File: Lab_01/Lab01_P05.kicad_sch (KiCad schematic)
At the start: 4 parts

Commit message: Edit Lab01 P5 Simulation
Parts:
- removed RLOAD1: 1000, symbol Device:R_Variable
- added R3: 1000, symbol Device:R
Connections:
- net GND: now also R3.2
- net Vout: now also R3.1
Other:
- note removed: ".tran 1u 1m"
- moved on the sheet: R1, R2, V_SUPPLY1

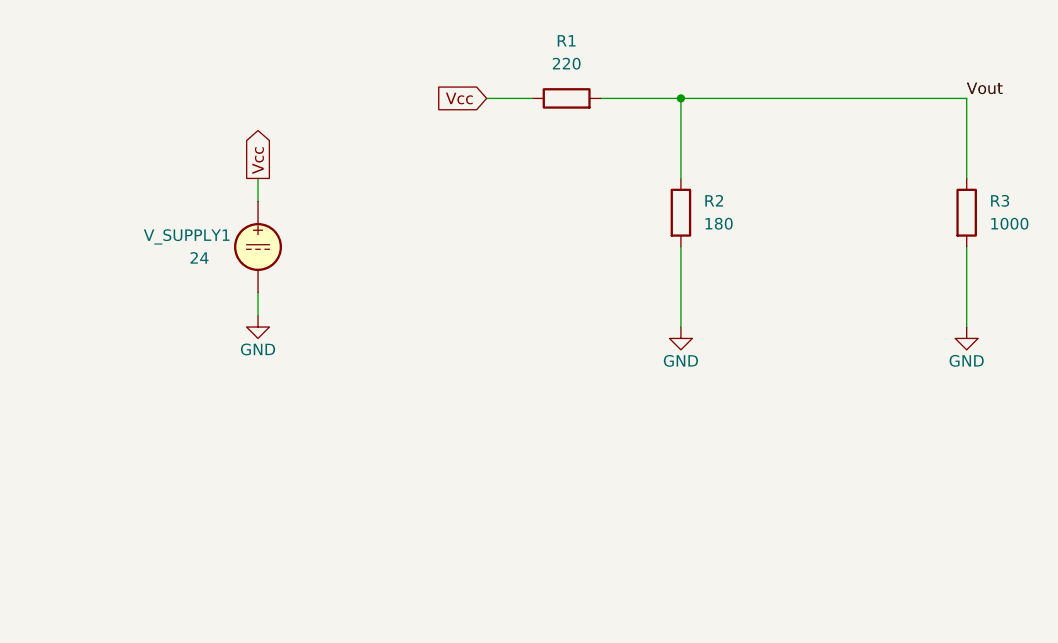
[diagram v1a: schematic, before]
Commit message: Capture and simulate P6&7 schemas
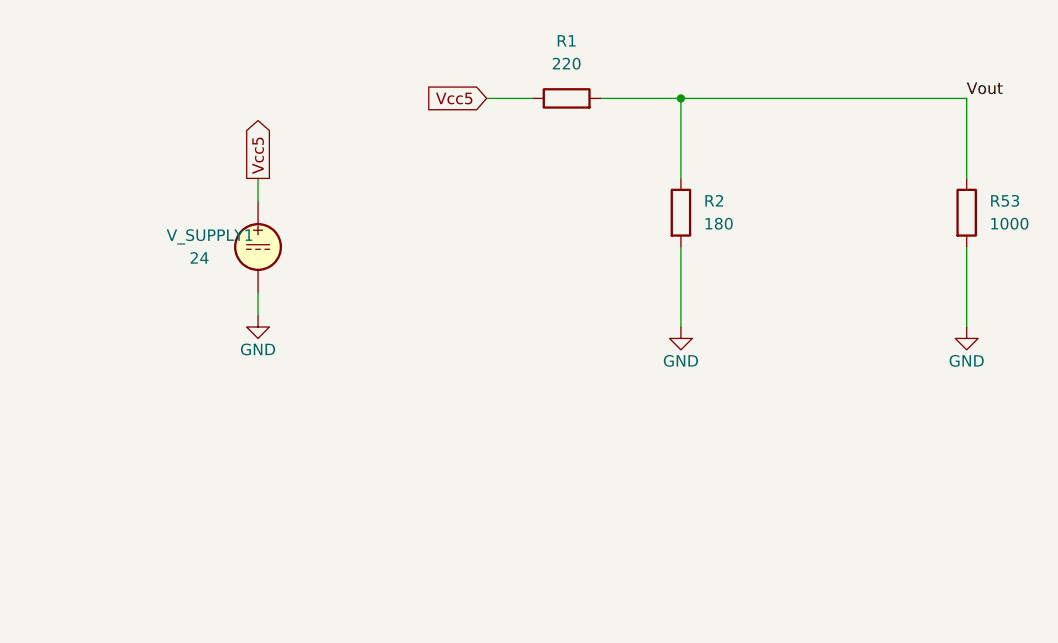
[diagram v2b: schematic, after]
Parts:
- renumbered R3 to R53
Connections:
- net Vcc renamed Vcc5
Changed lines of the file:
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@@
     (effects (font (size 1.27 1.27)) (justify left bottom))
   )
-  (global_label "Vcc" (shape output) (at 41.91 48.26 90) (fields_autoplaced)
+  (global_label "Vcc5" (shape output) (at 41.91 48.26 90) (fields_autoplaced)
     (effects (font (size 1.27 1.27)) (justify left))
-    (property "Intersheetrefs" "${INTERSHEET_REFS}" (at 41.91 42.0884 90)
+    (property "Intersheetrefs" "${INTERSHEET_REFS}" (at 41.91 40.8789 90)
       (effects (font (size 1.27 1.27)) (justify left) hide)
     )
   )
-  (global_label "Vcc" (shape input) (at 67.31 39.37 180) (fields_autoplaced)
+  (global_label "Vcc5" (shape input) (at 67.31 39.37 180) (fields_autoplaced)
     (effects (font (size 1.27 1.27)) (justify right))
-    (property "Intersheetrefs" "${INTERSHEET_REFS}" (at 61.1384 39.37 0)
+    (property "Intersheetrefs" "${INTERSHEET_REFS}" (at 59.9289 39.37 0)
       (effects (font (size 1.27 1.27)) (justify right) hide)
     )
@@
   (symbol (lib_id "Simulation_SPICE:VDC") (at 41.91 55.88 0) (unit 1)
     (in_bom yes) (on_board yes) (dnp no)
-    (property "Reference" "V_SUPPLY1" (at 29.21 54.61 0)
+    (property "Reference" "V_SUPPLY1" (at 31.75 54.61 0)
       (effects (font (size 1.27 1.27)) (justify left))
     )
@@
       (project "Lab01"
         (path "/f5e37932-d66b-45bd-afc2-f24a1a74700d/4efdc02f-e125-44e1-b96d-4aab0a060814"
-          (reference "V_SUPPLY1") (unit 1)
+          (reference "VDC51") (unit 1)
         )
       )
@@
   (symbol (lib_id "Device:R") (at 120.65 52.07 0) (unit 1)
     (in_bom yes) (on_board yes) (dnp no) (fields_autoplaced)
-    (property "Reference" "R3" (at 123.19 50.8 0)
+    (property "Reference" "R53" (at 123.19 50.8 0)
       (effects (font (size 1.27 1.27)) (justify left))
     )
@@
       (project "Lab01"
         (path "/f5e37932-d66b-45bd-afc2-f24a1a74700d/4efdc02f-e125-44e1-b96d-4aab0a060814"
-          (reference "R3") (unit 1)
+          (reference "R53") (unit 1)
         )
       )
@@
       (project "Lab01"
         (path "/f5e37932-d66b-45bd-afc2-f24a1a74700d/4efdc02f-e125-44e1-b96d-4aab0a060814"
-          (reference "R1") (unit 1)
+          (reference "R51") (unit 1)
         )
       )
@@
       (project "Lab01"
         (path "/f5e37932-d66b-45bd-afc2-f24a1a74700d/4efdc02f-e125-44e1-b96d-4aab0a060814"
-          (reference "R2") (unit 1)
+          (reference "R52") (unit 1)
         )
       )
